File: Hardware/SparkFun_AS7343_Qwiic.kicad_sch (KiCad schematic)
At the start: 38 parts, among them J1 Qwiic_RA, J2 Qwiic_RA, J3 Conn_01x06, Q1 BSS138, Q2 BSS138, U1 RT9080-1.8V, U2 AS7343

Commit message: fixed logic level converters
-body diodes in LLC transistors were allowing high side voltage into low side. (This was incorrect in v01).
-fixed LLC circuit to have low/high voltages on the correct sides
-rerouted
-bumped version to v02
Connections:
- net 1.8V: now also Q1.1 (G), Q2.1 (G)
- net 3.3V: no longer Q1.1 (G), Q2.1 (G)
- net SCL: now also Q1.3 (D); no longer Q1.2 (S)
- net SCL_1V8: now also Q1.2 (S); no longer Q1.3 (D)
- net SDA: now also Q2.3 (D); no longer Q2.2 (S)
- net SDA_1V8: now also Q2.2 (S); no longer Q2.3 (D)
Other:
- moved on the sheet: Q1, Q2, R4, R5, R7, R8

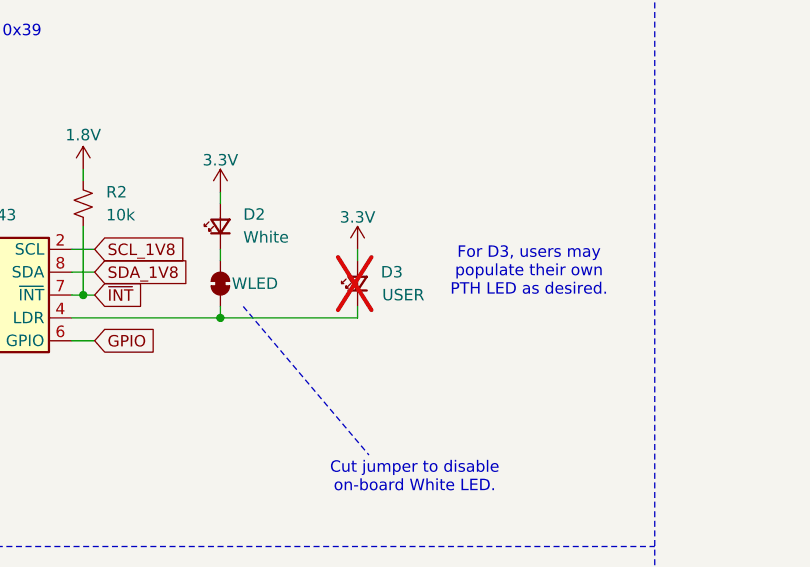
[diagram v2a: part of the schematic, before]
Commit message: eng checklist run for v10
-updated soldermask color to red
-library update on the DNP 5mm pth LED (linking due to new naming)
-library update on qwiic connector - looks like just an update on the courtyard
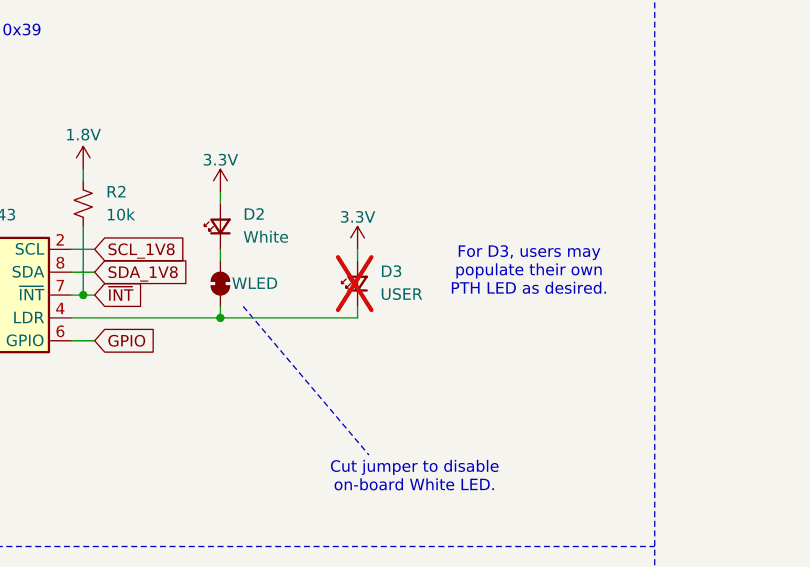
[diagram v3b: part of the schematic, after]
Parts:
- removed D3: USER, SparkFun-LED:LED_5MM, symbol SparkFun-LED:LED_Red_5mm_PTH
- added D3: USER, SparkFun-LED:LED_5mm_PTH_Red_NoSilk, symbol SparkFun-LED:LED_Red_5mm_PTH_NoSilk
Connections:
- net 3.3V: now also D3.2 (A)
- net at JP3.2 (B), U2.4 (LDR): now also D3.1 (K)
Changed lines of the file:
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@@
-	)
-	(symbol
-		(lib_id "SparkFun-LED:LED_Red_5mm_PTH")
-		(at 123.19 54.61 90)
-		(unit 1)
-		(exclude_from_sim no)
-		(in_bom yes)
-		(on_board yes)
-		(dnp yes)
-		(property "Reference" "D3"
-			(at 127 53.34 90)
-			(effects
-				(font
-					(size 1.27 1.27)
-				)
-			)
-		)
-		(property "Value" "USER"
-			(at 128.27 55.88 90)
-			(effects
-				(font
-					(size 1.27 1.27)
-				)
-			)
-		)
-		(property "Footprint" "SparkFun-LED:LED_5MM"
-			(at 128.27 54.61 0)
-			(effects
-				(font
-					(size 1.27 1.27)
-				)
-				(hide yes)
-			)
-		)
-		(property "Datasheet" "https://cdn.sparkfun.com/assets/e/c/e/c/5/COM-09590-YSL-R531R3D-D2.pdf"
-			(at 133.35 54.61 0)
-			(effects
-				(font
-					(size 1.27 1.27)
-				)
-				(hide yes)
-			)
-		)
-		(property "Description" "Light emitting diode PTH 5mm diameter"
-			(at 135.89 54.61 0)
-			(effects
-				(font
-					(size 1.27 1.27)
-				)
-				(hide yes)
-			)
-		)
-		(property "PROD_ID" "DIO-09529"
-			(at 130.81 54.61 0)
-			(effects
-				(font
-					(size 1.27 1.27)
-				)
-				(hide yes)
-			)
-		)
-		(pin "1"
-		)
-		(pin "2"
-		)
-		(instances
-			(project ""
-				(path "/e3dd3ae4-244d-4cba-9cca-5d2abf83f29a"
-					(reference "D3")
-					(unit 1)
-				)
-			)
-		)
 	)
 	(symbol
@@
 					(unit 1)
 				)
+			)
+		)
+	)
+	(symbol
+		(lib_id "SparkFun-LED:LED_Red_5mm_PTH_NoSilk")
+		(at 123.19 54.61 90)
+		(unit 1)
+		(exclude_from_sim no)
+		(in_bom yes)
+		(on_board yes)
+		(dnp yes)
+		(fields_autoplaced yes)
+		(property "Reference" "D3"
+			(at 125.73 53.2764 90)
+			(effects
+				(font
+					(size 1.27 1.27)
+				)
+				(justify right)
+			)
+		)
+		(property "Value" "USER"
+			(at 125.73 55.8164 90)
+			(effects
+				(font
+					(size 1.27 1.27)
+				)
+				(justify right)
+			)
+		)
+		(property "Footprint" "SparkFun-LED:LED_5mm_PTH_Red_NoSilk"
+			(at 128.27 54.61 0)
+			(effects
+				(font
+					(size 1.27 1.27)
+				)
+				(hide yes)
+			)
+		)
+		(property "Datasheet" "https://cdn.sparkfun.com/assets/e/c/e/c/5/COM-09590-YSL-R531R3D-D2.pdf"
+			(at 133.35 54.61 0)
+			(effects
+				(font
+					(size 1.27 1.27)
+				)
+				(hide yes)
+			)
+		)
+		(property "Description" "Light emitting diode PTH 5mm diameter"
+			(at 135.89 54.61 0)
+			(effects
+				(font
+					(size 1.27 1.27)
+				)
+				(hide yes)
+			)
+		)
+		(property "PROD_ID" "DIO-09529"
+			(at 130.81 54.61 0)
+			(effects
+				(font
+					(size 1.27 1.27)
+				)
+				(hide yes)
+			)
+		)
+		(pin "1"
+		)
+		(pin "2"
+		)
+		(instances
+			(project ""
+				(path "/e3dd3ae4-244d-4cba-9cca-5d2abf83f29a"
+					(reference "D3")
+					(unit 1)
+				)
